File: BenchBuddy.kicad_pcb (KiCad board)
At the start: 4 copper layers, 165.1 x 63.5 mm, 0 parts

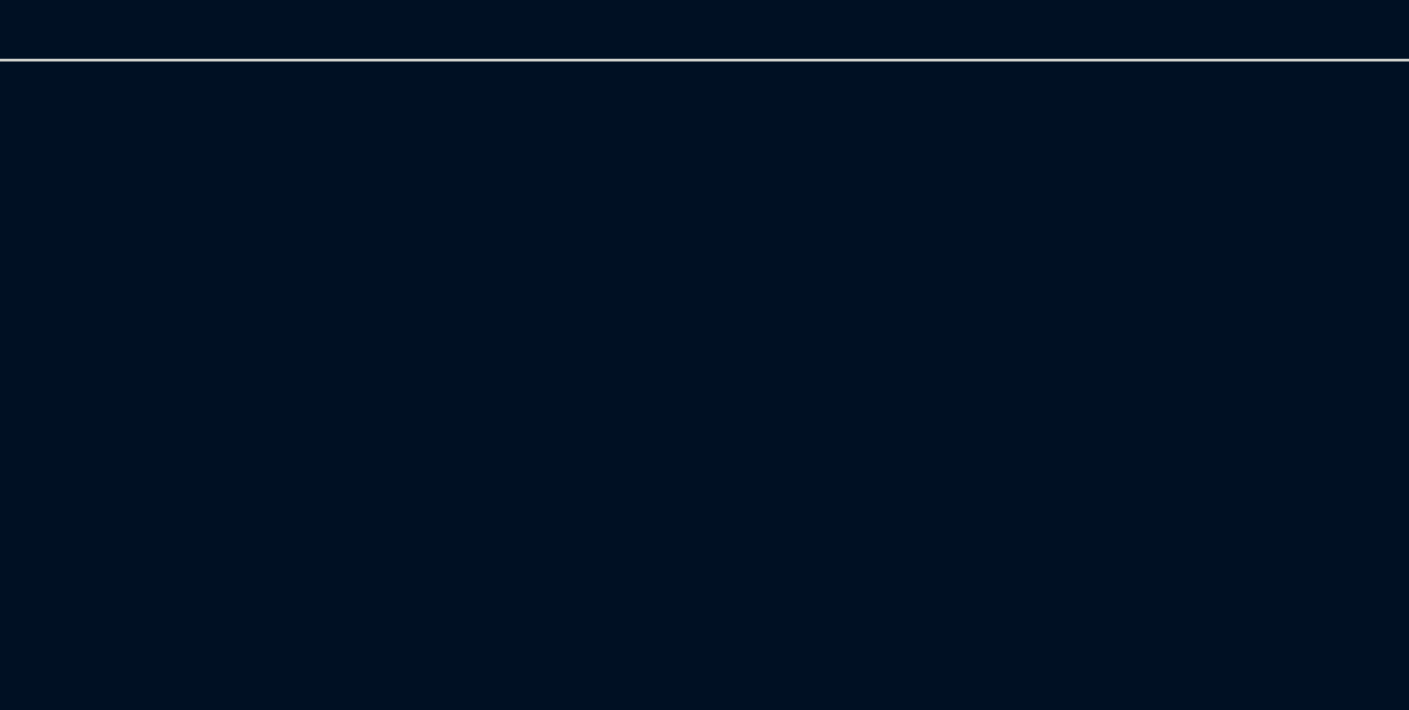
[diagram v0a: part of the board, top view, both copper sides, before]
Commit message: Associating and Placing the Relay Module
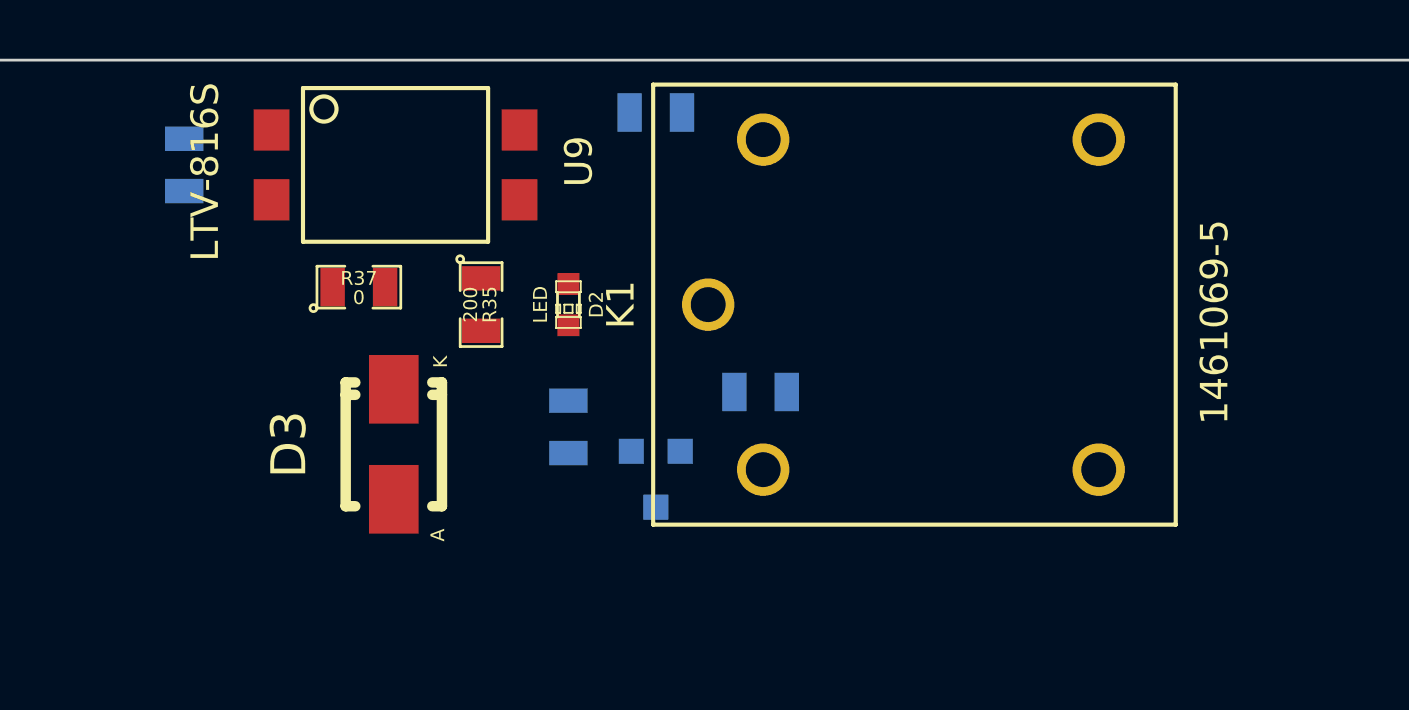
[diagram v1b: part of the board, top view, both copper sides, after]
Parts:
- added D2: LED, LEDs:LED-0603, F.Cu at (195.6, 64.8)
- added D3: B130-13-F, Diodes_SMD:Diode-SMA_Standard, F.Cu at (189.2, 69.8)
- added K1: 1461069-5, BenchBudEE:TE-SPDT_RELAY, F.Cu at (200.7, 64.8)
- added Q1: 2N3904, SMD_Packages:SOT23EBC, B.Cu at (198.8, 71.1)
- added R34: 500, SMD_Packages:SM0805, B.Cu at (181.6, 59.7)
- added R35: 200, SMD_Packages:SM0805, F.Cu at (192.4, 64.8)
- added R36: 100, SMD_Packages:SM0805, B.Cu at (195.6, 69.2)
- added R37: 0, SMD_Packages:SM0805, F.Cu at (188.0, 64.1)
- added R38: 0, SMD_Packages:SM0805, B.Cu at (198.8, 57.8)
- added R39: 0, SMD_Packages:SM0805, B.Cu at (202.6, 67.9)
- added U9: LTV-816S, BenchBudEE:SMD-4, F.Cu at (184.8, 58.4)

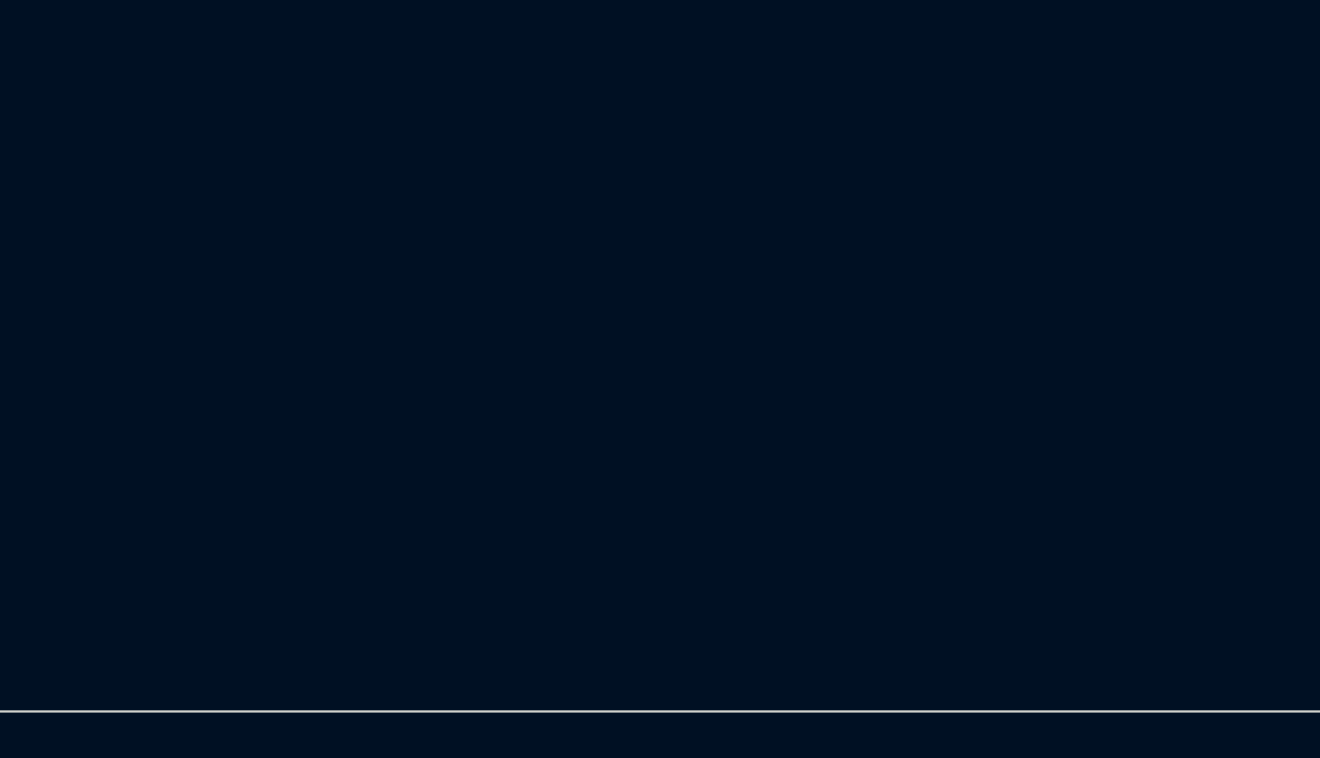
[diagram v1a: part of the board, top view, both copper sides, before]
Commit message: Associating and Placing the Thermocouple Module
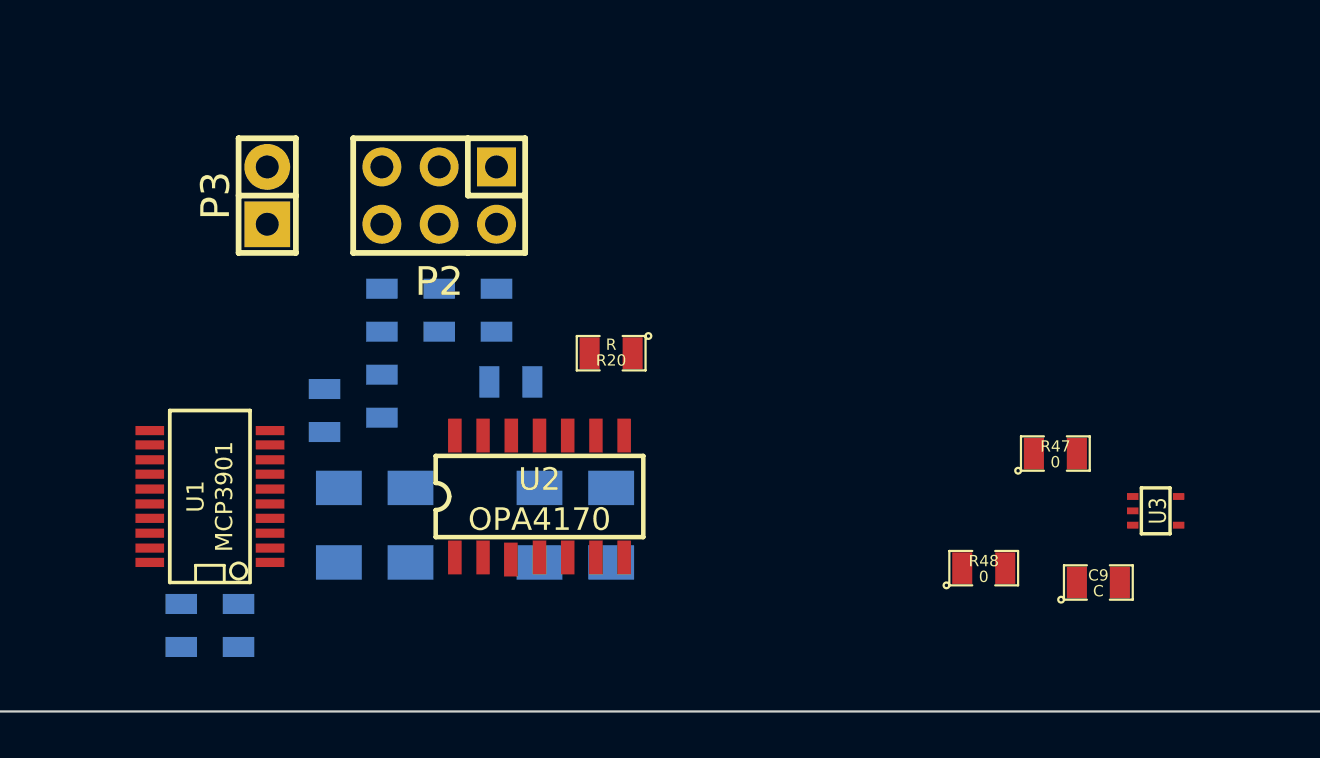
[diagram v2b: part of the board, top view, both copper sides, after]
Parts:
- added C1: C, SMD_Packages:SM0805, B.Cu at (182.9, 106.0)
- added C6: C, SMD_Packages:SM0805, B.Cu at (176.5, 115.6)
- added C7: C, SMD_Packages:SM0805, B.Cu at (179.1, 115.6)
- added C8: C, SMD_Packages:SM0805, B.Cu at (191.1, 104.8)
- added C9: C, SMD_Packages:SM0805, F.Cu at (217.2, 113.7)
- added P2: CONN_3X2, Pin_Headers:Pin_Header_Straight_2x03, F.Cu at (188.0, 96.5)
- added P3: CONN_2, Pin_Headers:Pin_Header_Straight_1x02, F.Cu at (180.3, 96.5)
- added R16: R, SMD_Packages:SM1206, B.Cu at (183.5, 111.1)
- added R17: R, SMD_Packages:SM1206, B.Cu at (186.7, 111.1)
- added R18: R, SMD_Packages:SM1206, B.Cu at (195.6, 111.1)
- added R19: R, SMD_Packages:SM1206, B.Cu at (192.4, 111.1)
- added R20: R, SMD_Packages:SM0805, F.Cu at (195.6, 103.5)
- added R21: R, SMD_Packages:SM0805, B.Cu at (190.5, 101.6)
- added R22: R, SMD_Packages:SM0805, B.Cu at (185.4, 105.4)
- added R43: R, SMD_Packages:SM0805, B.Cu at (185.4, 101.6)
- added R44: R, SMD_Packages:SM0805, B.Cu at (188.0, 101.6)
- added R47: 0, SMD_Packages:SM0805, F.Cu at (215.3, 108.0)
- added R48: 0, SMD_Packages:SM0805, F.Cu at (212.1, 113.0)
- added U1: MCP3901, SMD_Packages:SSOP20, F.Cu at (177.8, 109.9)
- added U2: OPA4170, SOIC_Packages:SOIC-14_Narrow, F.Cu at (192.4, 109.9)
- added U3: LMT84, SMD_Packages:SOT353, F.Cu at (219.7, 110.5)

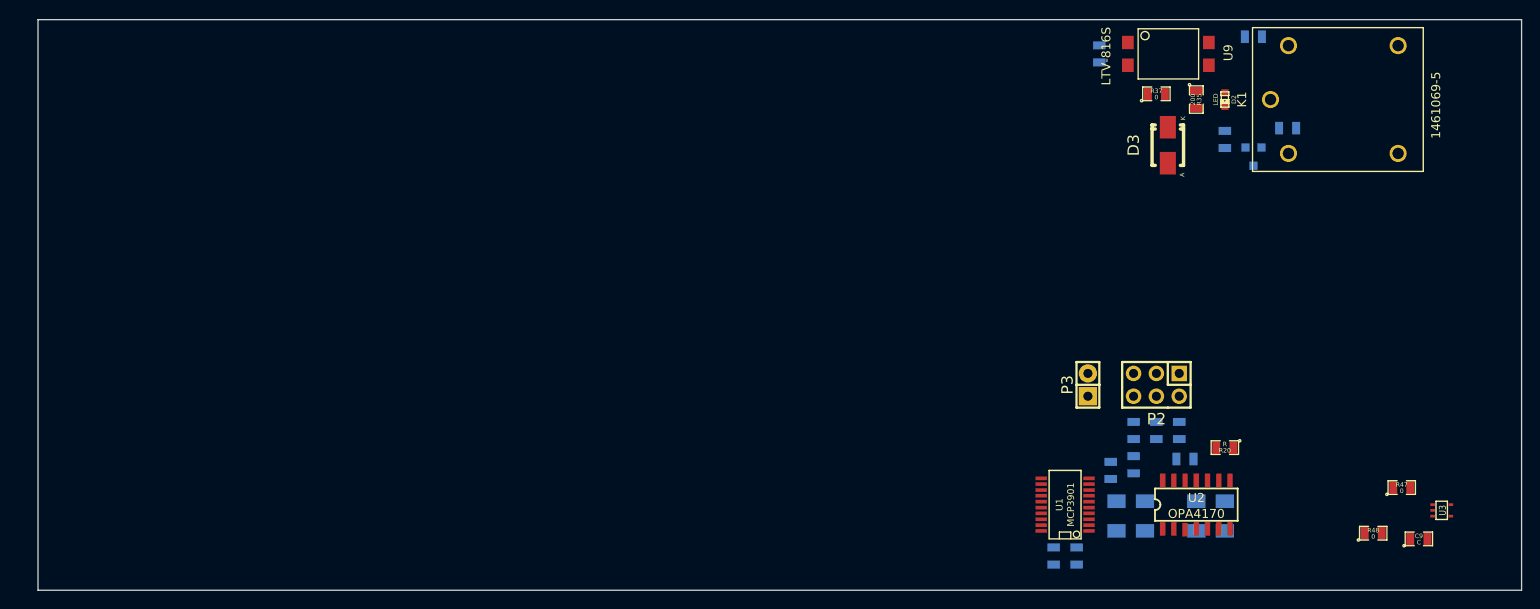
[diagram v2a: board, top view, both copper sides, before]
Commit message: Associating and Placing the Terminal/ATX Blocks
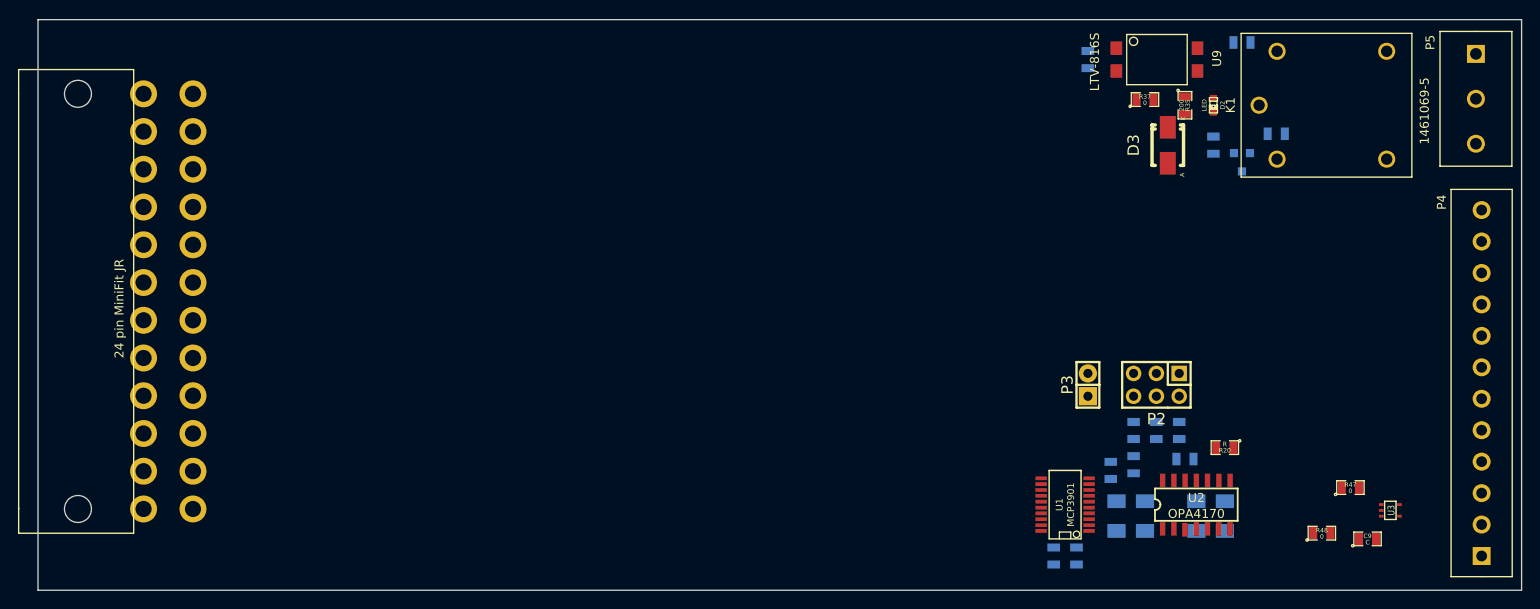
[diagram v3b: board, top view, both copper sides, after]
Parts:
- added P1: 24 pin MiniFit JR, BenchBudEE:ATX_HEADER, F.Cu at (67.9, 64.1)
- added P4: 12 pin Terminal Block, BenchBudEE:12_Pin_3.5mm_TB, F.Cu at (224.2, 115.6)
- added P5: 3 Pin TB, BenchBudEE:3_Pin_5mm_TB, F.Cu at (223.5, 59.7)
- moved R48 5.72 mm to (206.4, 113.0)
- moved U3 5.72 mm to (214.0, 110.5)
- moved C9 5.71 mm to (211.5, 113.7)
- moved R47 5.71 mm to (209.6, 108.0)
- moved D2 1.42 mm to (194.3, 65.4)
- moved K1 1.42 mm to (199.4, 65.4)
- moved R34 1.42 mm to (180.3, 60.3)
- moved R35 1.42 mm to (191.1, 65.4)
- moved R39 1.42 mm to (201.3, 68.6)
- moved U9 1.42 mm to (183.5, 59.1)
- moved R36 1.42 mm to (194.3, 69.8)
- moved R37 1.42 mm to (186.7, 64.8)
- moved R38 1.42 mm to (197.5, 58.4)
- moved Q1 1.42 mm to (197.5, 71.8)

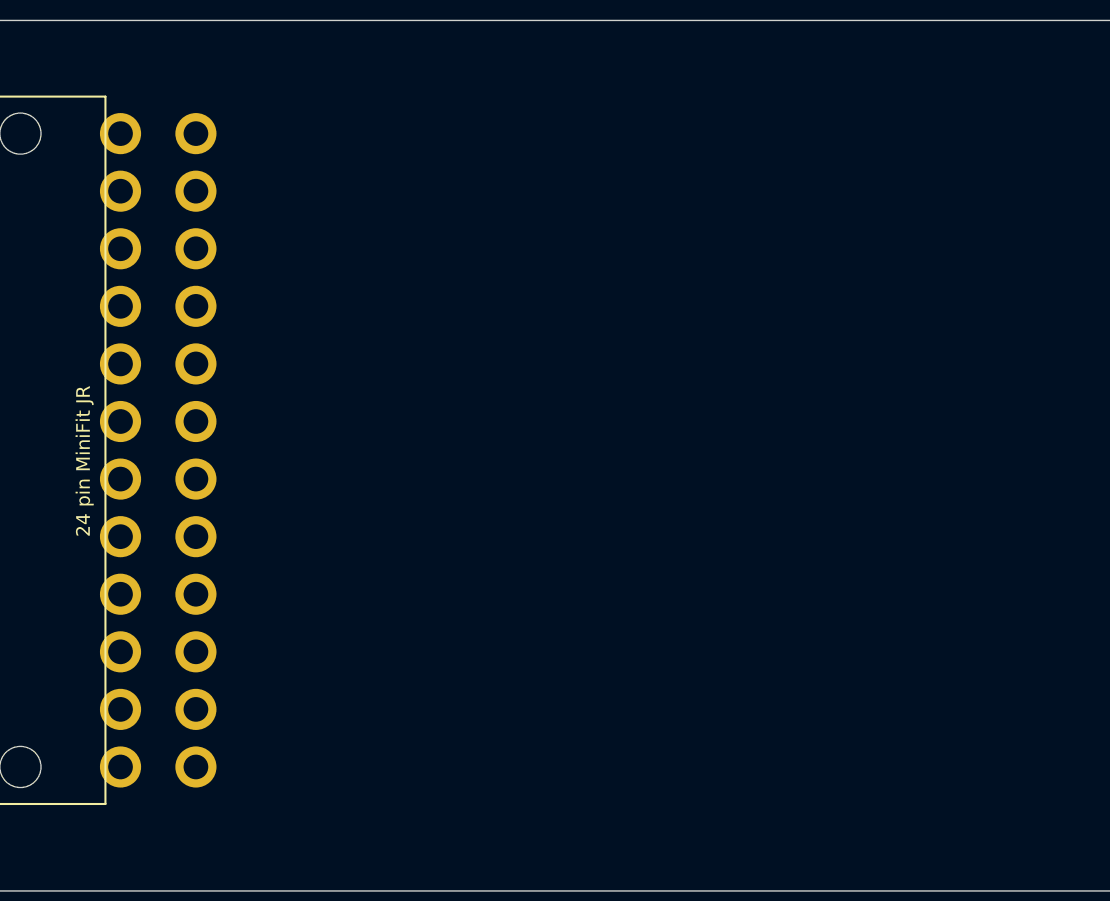
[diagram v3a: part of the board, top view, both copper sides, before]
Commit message: Associating and Placing the Arduino Module
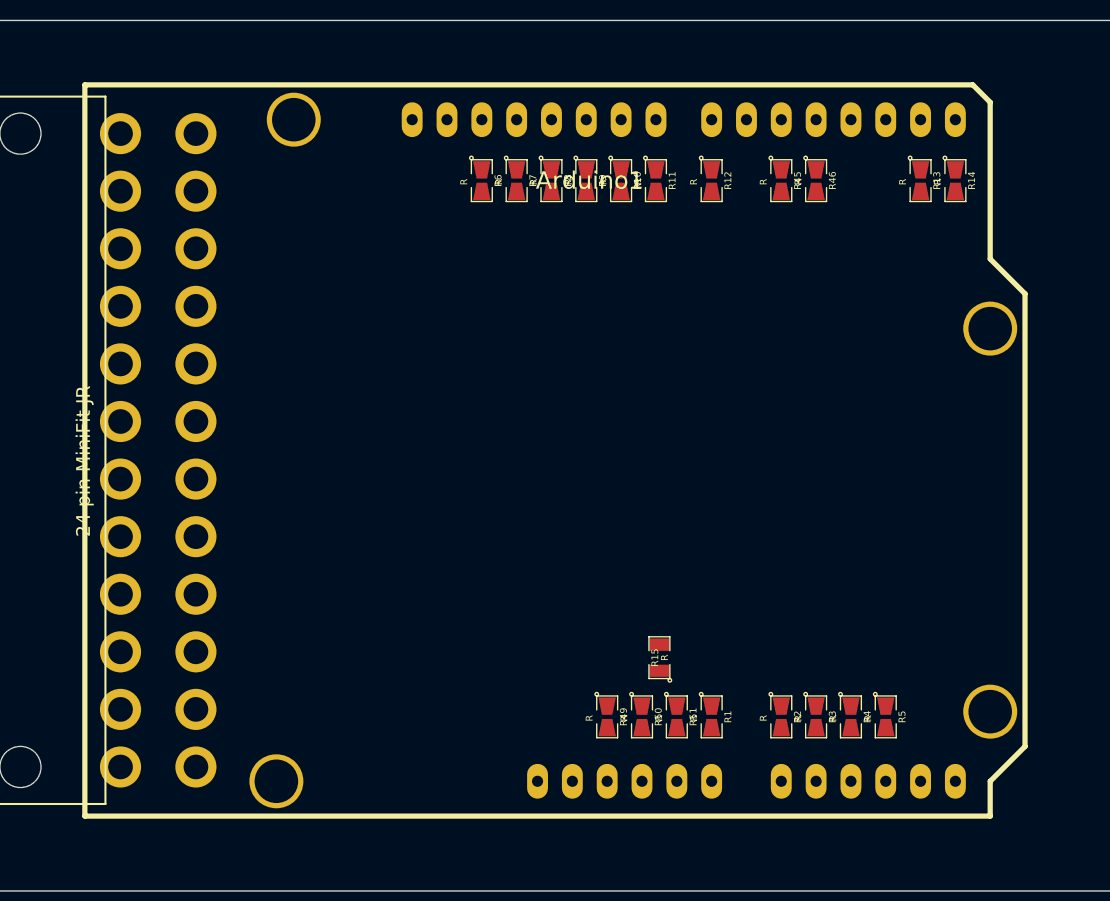
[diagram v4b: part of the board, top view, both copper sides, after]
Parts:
- added Arduino1: ARDUINO_SHIELD, Arduino:ARDUINO_SHIELD, F.Cu at (72.6, 113.9)
- added R1: R, BenchBudEE:SM0805-Bridge, F.Cu at (118.4, 106.7)
- added R10: R, BenchBudEE:SM0805-Bridge, F.Cu at (111.8, 67.6)
- added R11: R, BenchBudEE:SM0805-Bridge, F.Cu at (114.3, 67.6)
- added R12: R, BenchBudEE:SM0805-Bridge, F.Cu at (118.4, 67.6)
- added R13: R, BenchBudEE:SM0805-Bridge, F.Cu at (133.6, 67.6)
- added R14: R, BenchBudEE:SM0805-Bridge, F.Cu at (136.1, 67.6)
- added R15: R, SMD_Packages:SM0805, F.Cu at (114.6, 102.4)
- added R2: R, BenchBudEE:SM0805-Bridge, F.Cu at (123.4, 106.7)
- added R3: R, BenchBudEE:SM0805-Bridge, F.Cu at (126.0, 106.7)
- added R4: R, BenchBudEE:SM0805-Bridge, F.Cu at (128.5, 106.7)
- added R45: R, BenchBudEE:SM0805-Bridge, F.Cu at (123.4, 67.6)
- added R46: R, BenchBudEE:SM0805-Bridge, F.Cu at (126.0, 67.6)
- added R49: R, BenchBudEE:SM0805-Bridge, F.Cu at (110.7, 106.7)
- added R5: R, BenchBudEE:SM0805-Bridge, F.Cu at (131.1, 106.7)
- added R50: R, BenchBudEE:SM0805-Bridge, F.Cu at (113.3, 106.7)
- added R51: R, BenchBudEE:SM0805-Bridge, F.Cu at (115.8, 106.7)
- added R6: R, BenchBudEE:SM0805-Bridge, F.Cu at (101.6, 67.6)
- added R7: R, BenchBudEE:SM0805-Bridge, F.Cu at (104.1, 67.6)
- added R8: R, BenchBudEE:SM0805-Bridge, F.Cu at (106.7, 67.6)
- added R9: R, BenchBudEE:SM0805-Bridge, F.Cu at (109.2, 67.6)
